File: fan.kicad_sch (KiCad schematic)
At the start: 11 parts, among them J3 Conn_01x02_Pin, Q1 AO3400A, U4 LM393

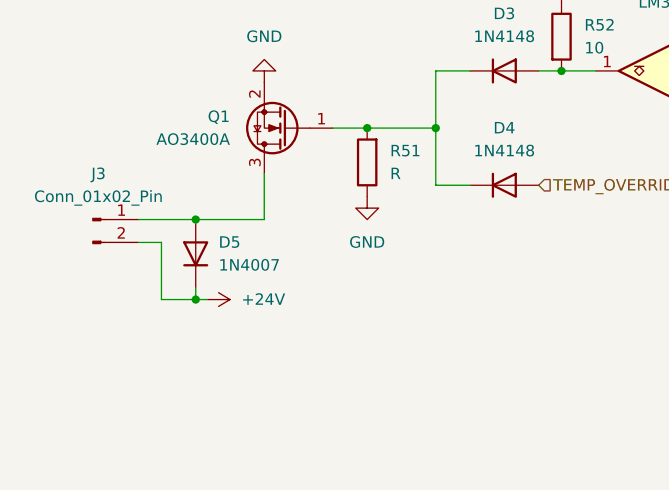
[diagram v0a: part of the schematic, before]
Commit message: Added some fan safety
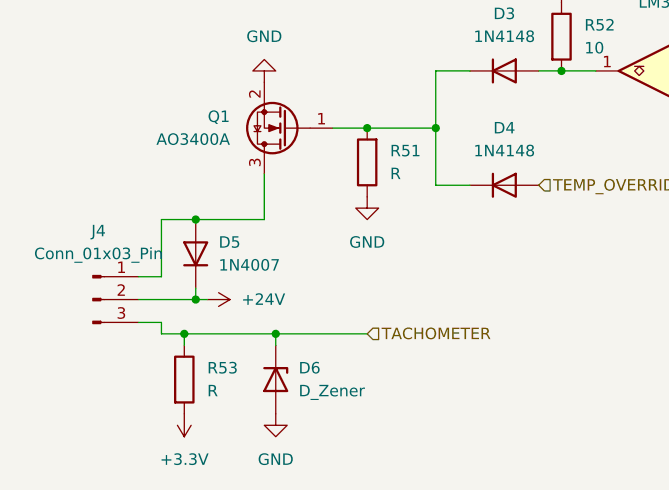
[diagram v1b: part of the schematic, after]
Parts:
- removed J3: Conn_01x02_Pin, symbol Connector:Conn_01x02_Pin
- added D6: D_Zener, symbol Device:D_Zener
- added J4: Conn_01x03_Pin, symbol Connector:Conn_01x03_Pin
- added R53: R, symbol Device:R
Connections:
- net +24V: now also J4.2 (Pin_2)
- net +3.3V: now also R53.2
- net GND: now also D6.2 (A)
- net at D5.2 (A), Q1.3 (D): now also J4.1 (Pin_1)
- new net TACHOMETER: D6.1 (K), J4.3 (Pin_3), R53.1

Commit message: Fixed most ERC checks
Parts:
- renumbered D5 to D3, D6 to D4, D3 to D5, D4 to D6, J4 to J27, R53 to R51, R51 to R52, R52 to R53, R50 to R54, U4 to U52
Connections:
- no-connect marks 0 -> 1
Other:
- moved on the sheet: U52B, U52C

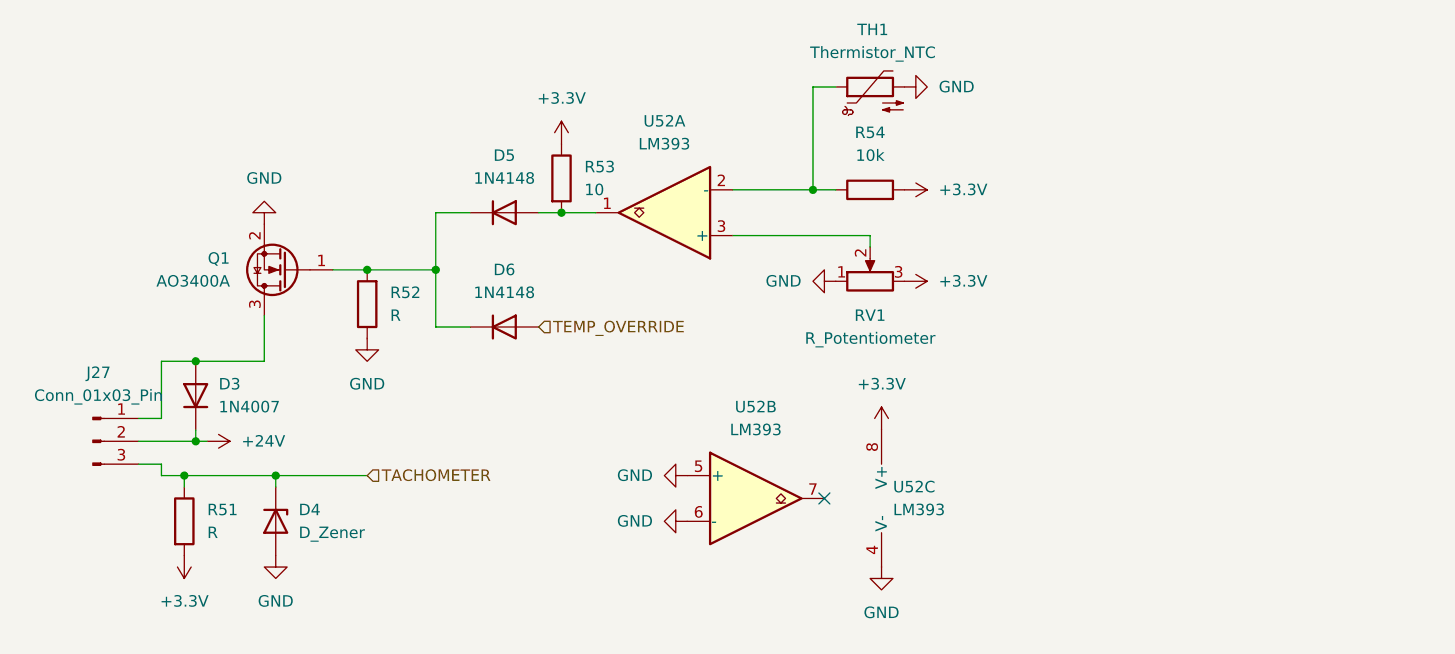
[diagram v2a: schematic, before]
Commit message: Footprinting done (warnings on schematic side but pcb import works fine)
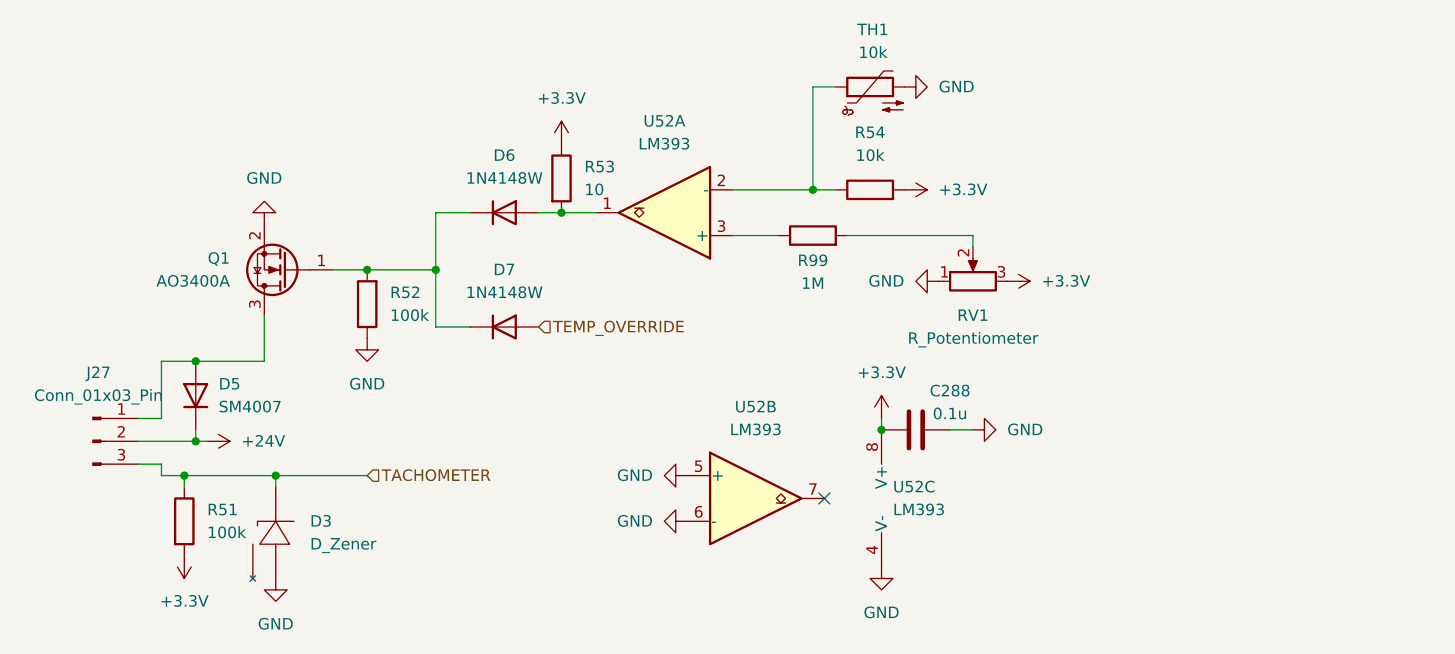
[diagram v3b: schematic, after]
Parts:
- removed D3: 1N4007, Diode_THT:D_DO-41_SOD81_P10.16mm_Horizontal, symbol Diode:1N4007
- removed D4: D_Zener, symbol Device:D_Zener
- removed D5, D6: 1N4148, Diode_THT:D_DO-35_SOD27_P7.62mm_Horizontal, symbol Diode:1N4148
- added C288: 0.1u, Capacitor_SMD:C_0603_1608Metric, symbol Device:C
- added D3: D_Zener, Diode_SMD:Zener_SOT-23_L2.9-W1.3-P1.90-LS2.4-BR, symbol D_Zener_BZX84:BZX84-C3V3,215
- added D5: SM4007, Diode_SMD:D_MELF, symbol Diode:SM4007
- added D6, D7: 1N4148W, Diode_SMD:D_SOD-123, symbol Diode:1N4148W
- added R99: 1M, Resistor_SMD:R_0603_1608Metric, symbol Device:R
- J27: footprint (none) -> Connector_Molex:Molex_KK-254_AE-6410-03A_1x03_P2.54mm_Vertical; LCSC Part # (none) -> C5333416
- R51, R52: value R -> 100k; footprint (none) -> Resistor_SMD:R_0603_1608Metric
- R53: footprint (none) -> Resistor_SMD:R_0805_2012Metric
- R54: footprint (none) -> Resistor_SMD:R_0603_1608Metric
- RV1: footprint (none) -> Potentiometer_THT:RES-ADJ-TH_3362P; LCSC Part # (none) -> C58159
- TH1: value Thermistor_NTC -> 10k; footprint (none) -> Resistor_SMD:R_0603_1608Metric; LCSC Part # (none) -> C5385
- U52: footprint (none) -> Package_SO:SOIC-8_3.9x4.9mm_P1.27mm; LCSC Part # (none) -> C32901
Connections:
- net +24V: now also D5.1 (K)
- net +3.3V: now also C288.1
- net GND: now also C288.2, D3.1 (A)
- net TACHOMETER: now also D3.3 (K)
- net TEMP_OVERRIDE: now also D7.2 (A)
- net at J27.1 (Pin_1), Q1.3 (D): now also D5.2 (A)
- net at Q1.1 (G), R52.2: now also D6.1 (K), D7.1 (K)
- net at R53.2, U52.1: now also D6.2 (A)
- net at U52.3 (+): now also R99.1; no longer RV1.2
- new net: R99.2, RV1.2
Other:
- moved on the sheet: RV1

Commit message: Minor schematic changes
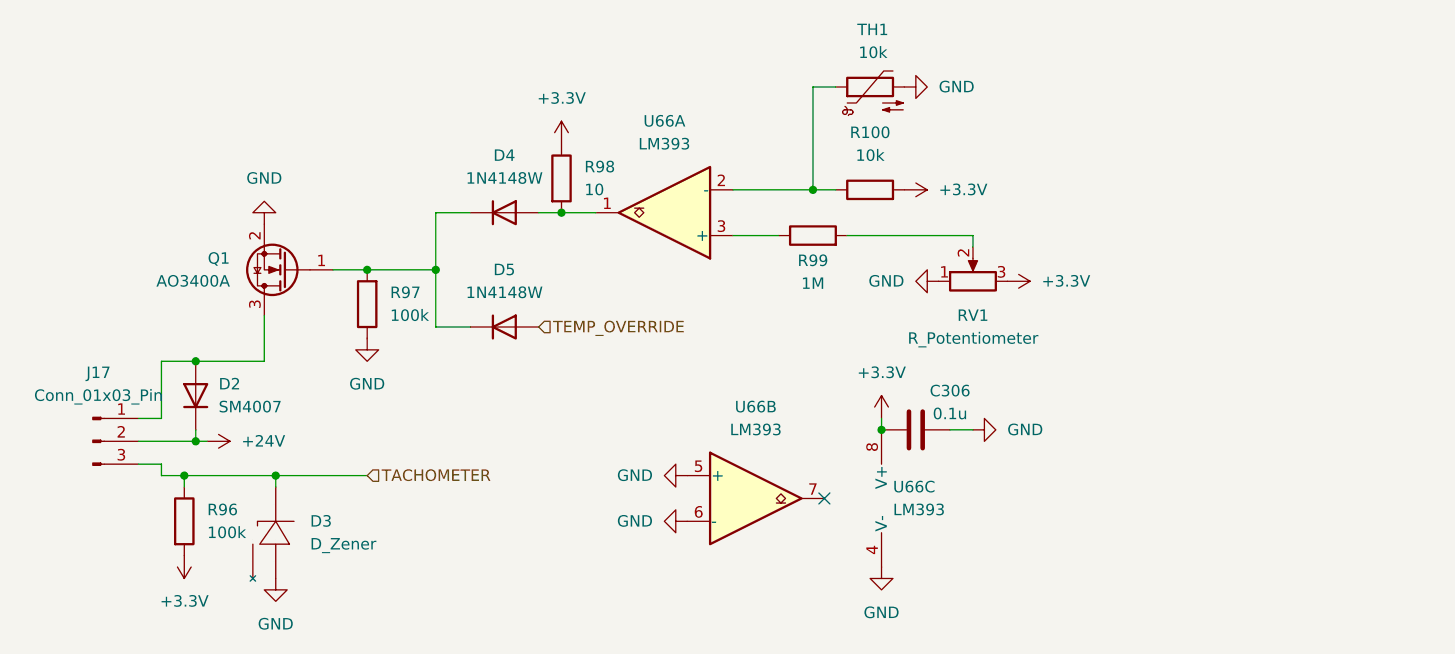
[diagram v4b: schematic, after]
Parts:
- renumbered C288 to C306, D5 to D2, D6 to D4, D7 to D5, J27 to J17, R54 to R100, R51 to R96, R52 to R97, R53 to R98, U52 to U66
